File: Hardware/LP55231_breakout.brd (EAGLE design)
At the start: 22.9 x 30.5 mm, 29 parts, among them J1 To micro, J2 USER LED, J3 USER LED, J4 USER LED, U1 LP55231WQFN

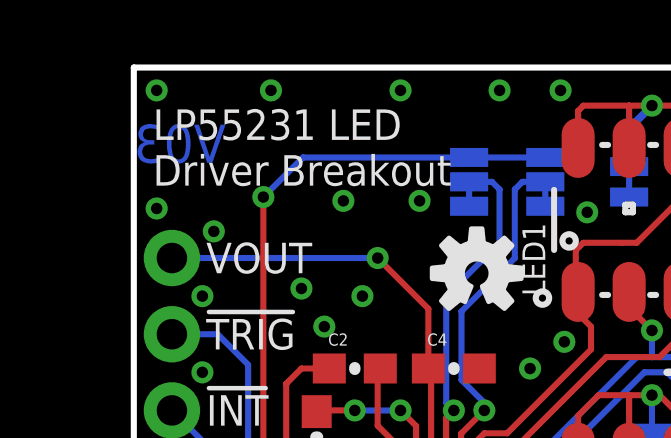
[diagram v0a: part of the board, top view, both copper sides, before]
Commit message: Making updates after group & checklist reviews.
Rolling version # to V10.
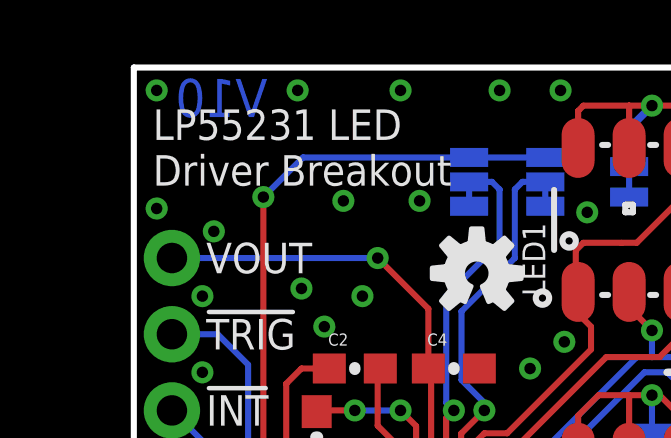
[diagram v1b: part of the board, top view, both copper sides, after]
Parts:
- moved LOGO1 3.81 mm to (7.24, 26.2)
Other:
- board text added: "V10"
- board text removed: "No!"
- board text removed: "V03"
- board text removed: "or"
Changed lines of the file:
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@@
 <layers>
 <layer number="1" name="Top" color="4" fill="1" visible="yes" active="yes"/>
-<layer number="2" name="Route2" color="1" fill="3" visible="no" active="no"/>
+<layer number="2" name="Route2" color="1" fill="3" visible="no" active="yes"/>
 <layer number="3" name="Route3" color="4" fill="3" visible="no" active="no"/>
 <layer number="4" name="Route4" color="1" fill="4" visible="no" active="no"/>
@@
 <layer number="13" name="Route13" color="4" fill="5" visible="no" active="no"/>
 <layer number="14" name="Route14" color="1" fill="6" visible="no" active="no"/>
-<layer number="15" name="Route15" color="4" fill="6" visible="no" active="no"/>
+<layer number="15" name="Route15" color="4" fill="6" visible="no" active="yes"/>
 <layer number="16" name="Bottom" color="1" fill="1" visible="yes" active="yes"/>
 <layer number="17" name="Pads" color="2" fill="1" visible="yes" active="yes"/>
@@
 <layer number="19" name="Unrouted" color="6" fill="1" visible="yes" active="yes"/>
 <layer number="20" name="Dimension" color="15" fill="1" visible="yes" active="yes"/>
-<layer number="21" name="tPlace" color="16" fill="1" visible="yes" active="yes"/>
+<layer number="21" name="tPlace" color="16" fill="1" visible="no" active="yes"/>
 <layer number="22" name="bPlace" color="14" fill="1" visible="yes" active="yes"/>
 <layer number="23" name="tOrigins" color="15" fill="1" visible="yes" active="yes"/>
@@
 <layer number="45" name="Holes" color="7" fill="1" visible="yes" active="yes"/>
 <layer number="46" name="Milling" color="3" fill="1" visible="no" active="yes"/>
-<layer number="47" name="Measures" color="7" fill="1" visible="no" active="yes"/>
+<layer number="47" name="Measures" color="7" fill="1" visible="yes" active="yes"/>
 <layer number="48" name="Document" color="7" fill="1" visible="no" active="yes"/>
 <layer number="49" name="Reference" color="7" fill="1" visible="no" active="yes"/>
@@
 <text x="2.413" y="21.59" size="1.016" layer="21" font="vector" ratio="15" rot="R180" align="center-right">!TRIG</text>
 <text x="2.413" y="24.13" size="1.016" layer="21" font="vector" ratio="15" rot="R180" align="center-right">VOUT</text>
-<text x="0" y="27.94" size="1.27" layer="16" font="vector" ratio="15" rot="MR0" align="center-right">V03</text>
+<text x="2.921" y="30.099" size="1.27" layer="16" font="vector" ratio="15" rot="MR0" align="top-center">V10</text>
 <text x="2.413" y="8.89" size="1.016" layer="22" font="vector" ratio="15" rot="MR0" align="center-right">VCC</text>
 <text x="2.413" y="11.43" size="1.016" layer="22" font="vector" ratio="15" rot="MR0" align="center-right">SDA</text>
@@
 <dimension x1="0" y1="30.48" x2="22.86" y2="30.48" x3="11.43" y3="35.56" textsize="1.016" textratio="15" layer="47" unit="inch"/>
 <text x="2.54" y="38.1" size="1.016" layer="47" font="vector" ratio="15">All Dimensions In Inches</text>
-<rectangle x1="9.0678" y1="13.7922" x2="9.8298" y2="13.843" layer="41"/>
+<rectangle x1="8.0518" y1="13.7922" x2="8.8138" y2="13.843" layer="41"/>
 <text x="16.383" y="3.81" size="1.016" layer="22" font="vector" ratio="15" rot="MR180" align="top-center">D3</text>
-<text x="7.62" y="15.367" size="1.016" layer="22" font="vector" ratio="15" rot="MR180" align="center-right">No!</text>
-<wire x1="9.017" y1="14.478" x2="8.001" y2="14.478" width="0.2032" layer="22"/>
-<wire x1="8.001" y1="16.002" x2="9.017" y2="16.002" width="0.2032" layer="22"/>
-<wire x1="9.017" y1="16.002" x2="9.017" y2="14.478" width="0.2032" layer="22"/>
-<wire x1="8.001" y1="14.478" x2="8.001" y2="16.002" width="0.2032" layer="22"/>
-<rectangle x1="8.001" y1="14.478" x2="9.017" y2="16.002" layer="22"/>
-<wire x1="11.43" y1="14.478" x2="12.446" y2="14.478" width="0.2032" layer="22"/>
-<wire x1="12.446" y1="16.002" x2="11.43" y2="16.002" width="0.2032" layer="22"/>
-<wire x1="11.43" y1="16.002" x2="11.43" y2="14.478" width="0.2032" layer="22"/>
-<wire x1="12.446" y1="16.002" x2="12.446" y2="14.478" width="0.2032" layer="22"/>
-<text x="10.922" y="15.367" size="1.016" layer="22" font="vector" ratio="15" rot="MR180" align="center-right">or</text>
 </plain>
 <attributes>
@@
 </class>
 </classes>
-<designrules name="SparkFun-2-layer-TIGHT">
-<description language="en">&lt;b&gt;SparkFun 2 Layer Design Rule Checks - STANDARD/TIGHT/FAB-LIMIT&lt;/b&gt;
+<designrules name="SparkFun-4-layer-TIGHT">
+<description language="en">&lt;b&gt;EAGLE Design Rules&lt;/b&gt;
 &lt;p&gt;
-These rules have been curated by SparkFuns DFM commitee. After doing much research, communicating with our multiple fab houses, and getting quotes of various designs, we have compiled three DRU files.
-&lt;p&gt;
-&lt;b&gt;STANDARD:&lt;/b&gt; This is more of a &quot;best case scenario&quot; set of limitations. If your design has the space, and/or you have the time to work within these parameters, please do. Larger trace width and clearance makes for easier visual inspection of the PCB while troubleshooting (useful in production and to the end user). It also allows for better ability to hack a trace (if you are crazy enough to scrape away the mask and solder to a trace). Another thing to keep in mind is that more metal is just more robust.
-&lt;p&gt;
-&lt;b&gt;TIGHT:&lt;/b&gt; This is where cost comes into play. We have found that most fab houses begin to add extra charges when you go smaller than these specs. In some cases, going to less than 15 mil trace can increase the cost by 10%. (This is why we have set the min drill on this DRU to 15 mil) Same story for traces thinner than 7 mil. To avoid those extra charges, then stay within the rules of this DRU.
-&lt;p&gt;
-&lt;b&gt;FAB-LIMIT:&lt;/b&gt; These set of rules are at the very limit of most fab houses capabilities. You will pay more for these specs, and it should be used on designs that have a darned good reason to need 4 mil vias and 4 mil traces.
-&lt;p&gt;
-**NOTE Clearance, Distance, Sizes, and Restring are all set to different limits in each of these three DRU files. Please compare the files within the CAM job editor window of eagle to see all the numbers.
-&lt;p&gt;
-***NOTE, Please set your Net Classes to default (0mil for all settings), so that it won't effect the DRC when you run it with these settings.</description>
-<param name="layerSetup" value="(1*16)"/>
-<param name="mtCopper" value="0.035mm 0.035mm 0.035mm 0.035mm 0.035mm 0.035mm 0.035mm 0.035mm 0.035mm 0.035mm 0.035mm 0.035mm 0.035mm 0.035mm 0.035mm 0.035mm"/>
-<param name="mtIsolate" value="1.5mm 0.15mm 0.2mm 0.15mm 0.2mm 0.15mm 0.2mm 0.15mm 0.2mm 0.15mm 0.2mm 0.15mm 0.2mm 0.15mm 0.2mm"/>
+The default Design Rules have been set to cover
+a wide range of applications. Your particular design
+may have different requirements, so please make the
+necessary adjustments and save your customized
+design rules under a new name.</description>
+<param name="layerSetup" value="(1*2*15*16)"/>
+<param name="mtCopper" value="0.035559375mm 0.035559375mm 0.035mm 0.035mm 0.035mm 0.035mm 0.035mm 0.035mm 0.035mm 0.035mm 0.035mm 0.035mm 0.035mm 0.035mm 0.035559375mm 0.035559375mm"/>
+<param name="mtIsolate" value="0.47751875mm 0.47751875mm 0.2mm 0.15mm 0.2mm 0.15mm 0.2mm 0.15mm 0.2mm 0.15mm 0.2mm 0.15mm 0.2mm 0.15mm 0.47751875mm"/>
 <param name="mdWireWire" value="7mil"/>
 <param name="mdWirePad" value="7mil"/>
@@
 <attribute name="PROD_ID" value="RES-09117" x="5.842" y="6.858" size="1.778" layer="27" font="vector" ratio="15" rot="R270" display="off"/>
 </element>
-<element name="LOGO1" library="SparkFun-Aesthetics" package="SFE_LOGO_FLAME_.1" value="SFE_LOGO_FLAME.1_INCH" x="3.429" y="26.162" rot="MR0"/>
+<element name="LOGO1" library="SparkFun-Aesthetics" package="SFE_LOGO_FLAME_.1" value="SFE_LOGO_FLAME.1_INCH" x="7.239" y="26.162" rot="MR0"/>
 <element name="LED2" library="SparkFun-LED" package="LED-TRICOLOR-5050" value="TRICOLOR-5050" x="16.51" y="15.24" rot="R90">
 <attribute name="PROD_ID" value="DIO-10298" x="16.51" y="15.24" size="1.778" layer="27" rot="R90" display="off"/>
@@
 <wire x1="8.164" y1="14.986" x2="9.136" y2="14.986" width="0.2032" layer="1"/>
 <wire x1="9.136" y1="14.986" x2="9.14" y2="14.99" width="0.2032" layer="1"/>
-<via x="4.572" y="29.718" extent="1-16" drill="0.381"/>
+<via x="5.461" y="29.718" extent="1-16" drill="0.381"/>
 <via x="14.351" y="21.336" extent="1-16" drill="0.381"/>
 <via x="20.574" y="22.86" extent="1-16" drill="0.381"/>
